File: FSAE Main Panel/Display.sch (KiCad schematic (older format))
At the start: 92 parts, among them Q501 SI2308CDS-T1-GE3, Q502 SI2308CDS-T1-GE3, U501 TLC6C598, U502 TLC6C5816, U503 TLC6C5816, U504 TLC6C5816

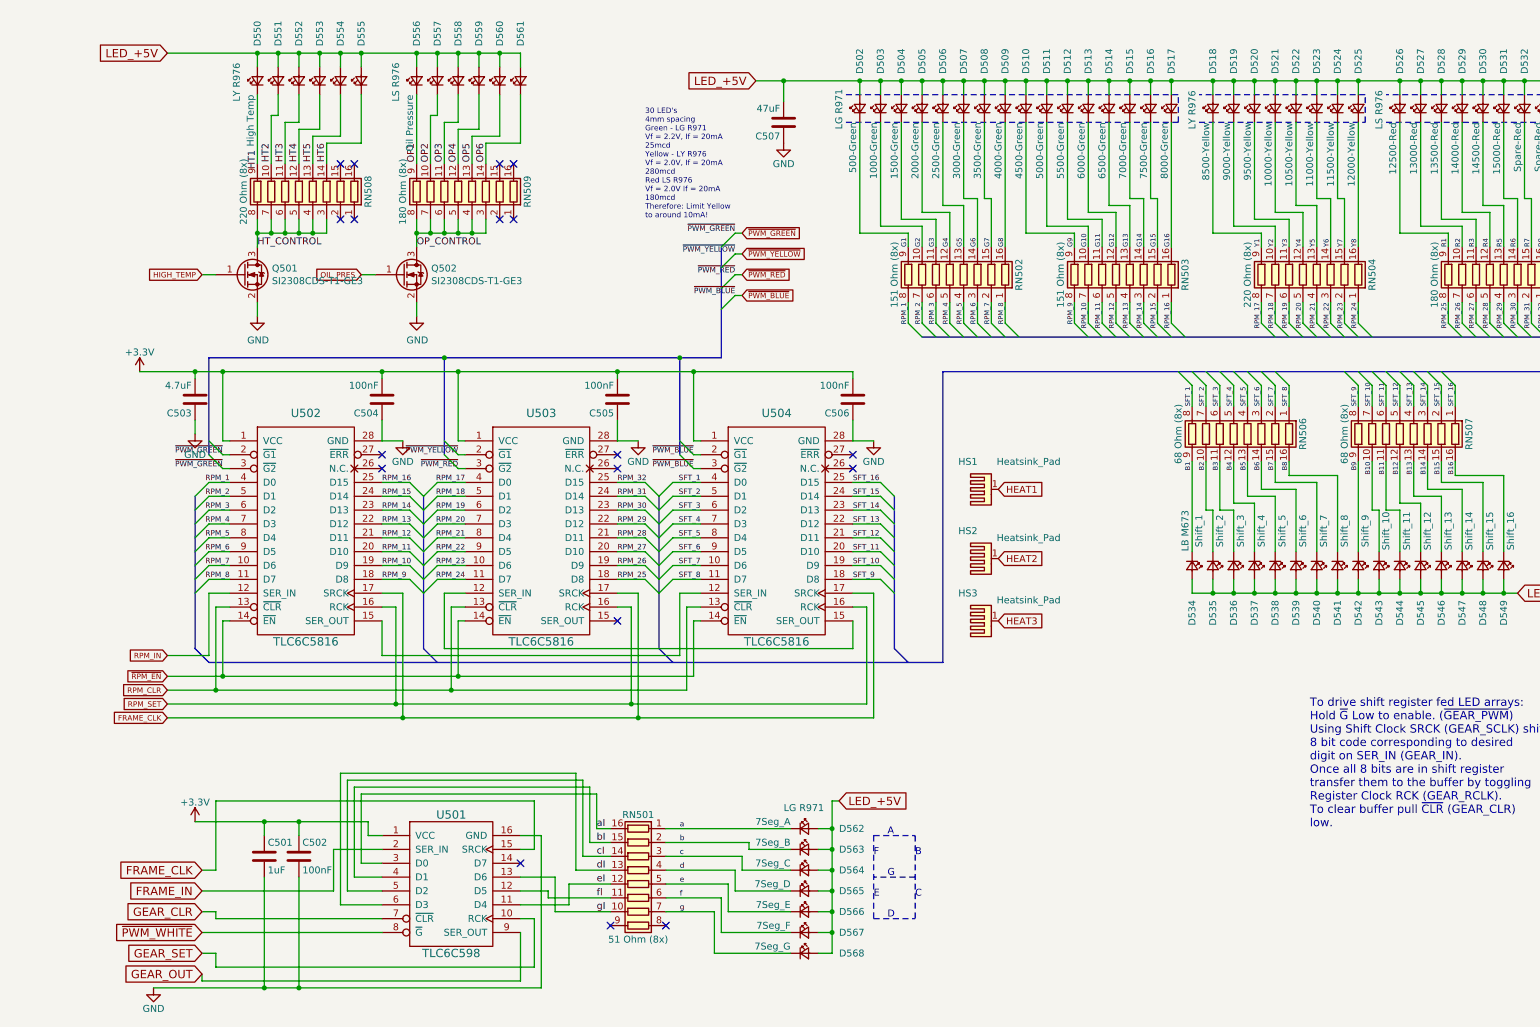
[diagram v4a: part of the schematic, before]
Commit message: Updated attributes and BOM
Standardized the component attributes and BOM.

Some errors were identified and will be corrected in the next board revision
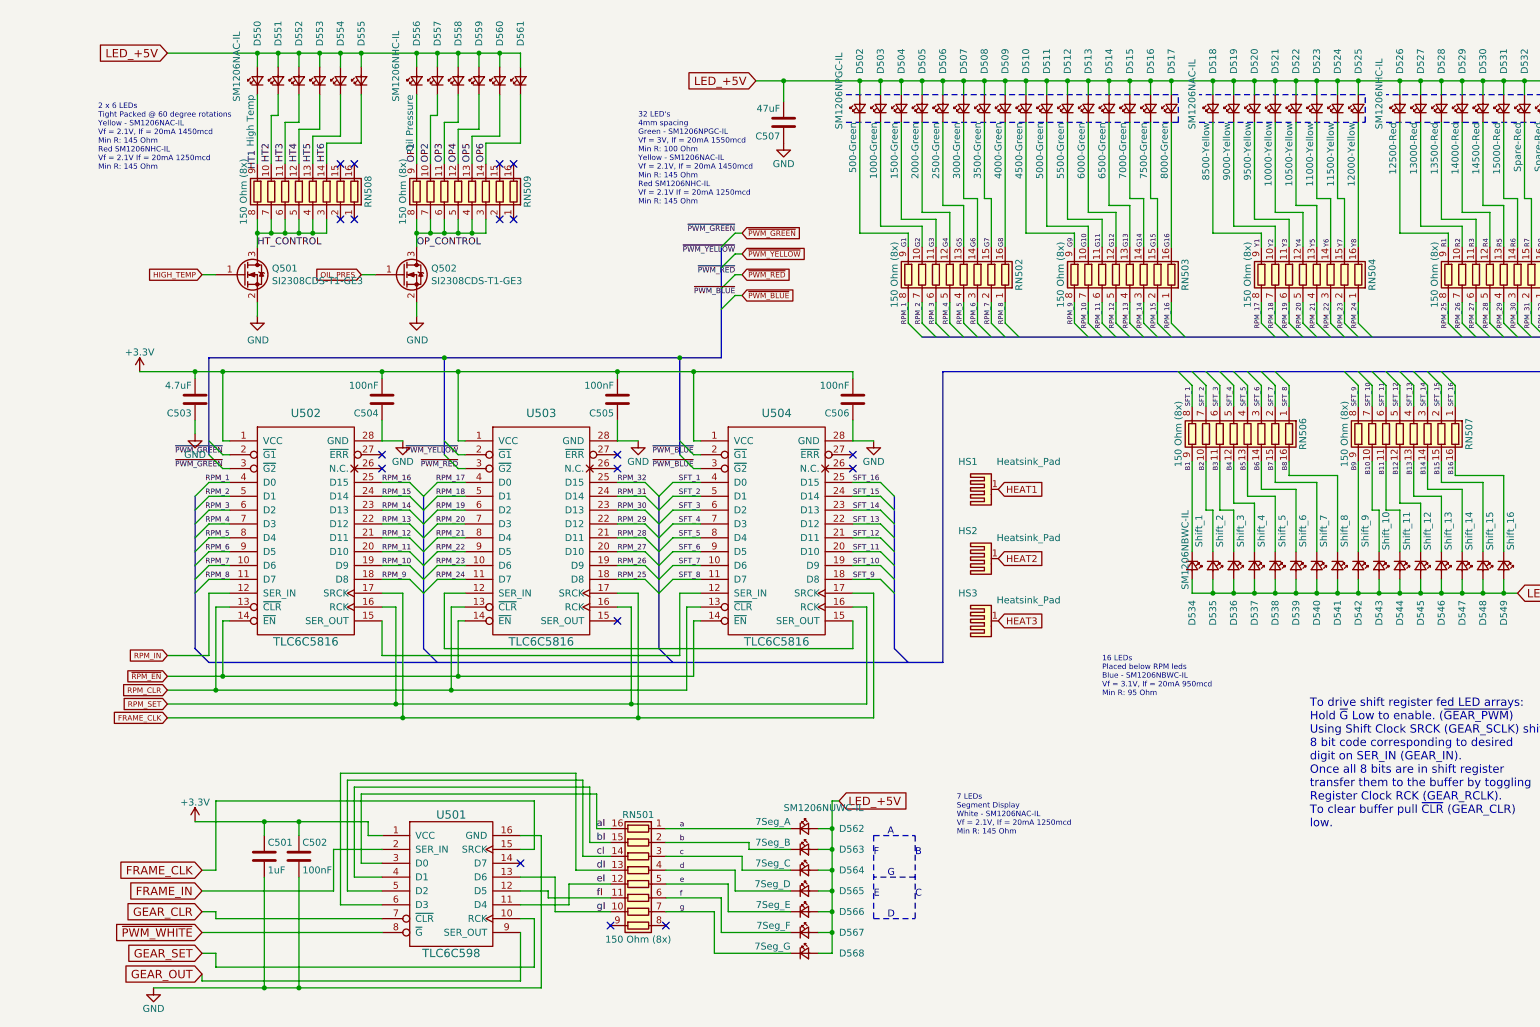
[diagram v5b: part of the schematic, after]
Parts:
- C501: Description Ceramic 1uF 25V X7R 1206 -> CAP CER 1UF 25V X5R 1206; Manufacturer (none) -> KEMET; Part Number (none) -> C1206C105K3PACTU
- C502, C504, C505, C506: Description Ceramic 0.1uF 10V X7R 1206 -> CAP CER 0.1UF 25V X7R 1206; Manufacturer (none) -> KEMET; Part Number (none) -> C1206F104K3RACTU
- C503: Description Ceramic 4.7uF 10V X5R 1206 -> CAP CER 4.7UF 25V X5R 1206; Manufacturer (none) -> KEMET; Part Number (none) -> C1206C475K3PACTU
- C507: Description Ceramic 47uF 10V X5R 1206 -> CAP CER 47UF 10V X5R 1206; Manufacturer (none) -> Murata; Part Number (none) -> GRT31CR61A476KE13L
- D502, D503, D504, D505, D506, D507, D508, D509, D510, D511, D512, D513, D514, D515, D516, D517: value LG R971 -> SM1206NPGC-IL; Description (none) -> LED GREEN CLEAR 1206 SMD; Manufacturer Kingbright -> Bivar; Part Number APD3224ZGCK-F01 -> SM1206NPGC-IL
- D518, D519, D520, D521, D522, D523, D524, D525, D550, D551, D552, D553, D554, D555: value LY R976 -> SM1206NAC-IL; Description (none) -> LED AMBER CLEAR 1206 SMD; Manufacturer Kingbright -> Bivar; Part Number (none) -> SM1206NAC-IL
- D526, D527, D528, D529, D530, D531, D532, D533, D556, D557, D558, D559, D560, D561: value LS R976 -> SM1206NHC-IL; Manufacturer Kingbright -> Bivar
- D534, D535, D536, D537, D538, D539, D540, D541, D542, D543, D544, D545, D546, D547, D548, D549: value LB M673 -> SM1206NBWC-IL; Description (none) -> LED BLUE CLEAR 1206 SMD; Manufacturer Kingbright -> Bivar; Part Number (none) -> SM1206NBWC-IL
- D562, D563, D564, D565, D566, D567, D568: value LG R971 -> SM1206NUWC-IL; Description (none) -> LED WHITE DIFFUSED 1206 SMD; Manufacturer Kingbright -> Bivar; Part Number APD3224ZGCK-F01 -> SM1206NUWC-IL
- HS1, HS2, HS3: Description (none) -> Pad for routing; Manufacturer (none) -> N/A; Part Number (none) -> N/A
- Q501, Q502: Description (none) -> MOSFET N-CH 60V 2.6A SOT23-3; Manufacturer (none) -> Vishay; Part Number (none) -> SI2308CDS-T1-GE3
- RN501: value 51 Ohm (8x) -> 150 Ohm (8x); footprint Housings_SOIC:SOIC-16_3.9x9.9mm_Pitch1.27mm -> Bourns 4800P:Bourns 4800P SOM-16; Description (none) -> RES ARRAY 8 RES 150 OHM 16SOIC; Manufacturer (none) -> Bourns; Part Number 4816P-1-510LF -> 4816P-1-151LF
- RN502, RN503: value 151 Ohm (8x) -> 150 Ohm (8x); Description (none) -> RES ARRAY 8 RES 150 OHM 16SOIC; Manufacturer (none) -> Bourns; Part Number 4816P-1-151 -> 4816P-1-151LF
- RN504, RN508: value 220 Ohm (8x) -> 150 Ohm (8x); Description (none) -> RES ARRAY 8 RES 150 OHM 16SOIC; Manufacturer (none) -> Bourns; Part Number 4816P-1-221LF -> 4816P-1-151LF
- RN505, RN509: value 180 Ohm (8x) -> 150 Ohm (8x); Description (none) -> RES ARRAY 8 RES 150 OHM 16SOIC; Manufacturer (none) -> Bourns; Part Number 4816P-1-181LF -> 4816P-1-151LF
- RN506, RN507: value 68 Ohm (8x) -> 150 Ohm (8x); Description (none) -> RES ARRAY 8 RES 150 OHM 16SOIC; Manufacturer (none) -> Bourns; Part Number 4816P-1-680LF -> 4816P-1-151LF
- U501: Description (none) -> IC LED DRIVER PS 50MA 16TSSOP; Manufacturer Texas Instruments -> TI; Part Number (none) -> TLC6C598QPWRQ1
- U502, U503, U504: Description (none) -> TLC6C5816 PROD VERSION; Manufacturer (none) -> TI; Part Number (none) -> TLC6C5816QPWPRQ1
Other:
- note added: "16 LEDs\nPlaced below RPM leds\nBlue - SM1206NBWC-IL\nVf = 3.1V, If = 20mA 950mcd\nMin R: 95 Ohm\n"
- note added: "2 x 6 LEDs\nTight Packed @ 60 degree rotations\nYellow - SM1206NAC-IL\nVf = 2.1V, If = 20mA 1450mcd\nMin R: 145 Ohm\nRed SM1206NHC-IL\nVf = 2.1V If = 20mA 1250mcd\nMin R: 145 Ohm"
- note added: "32 LED's\n4mm spacing\nGreen - SM1206NPGC-IL\nVf = 3V, If = 20mA 1550mcd\nMin R: 100 Ohm\nYellow - SM1206NAC-IL\nVf = 2.1V, If = 20mA 1450mcd\nMin R: 145 Ohm\nRed SM1206NHC-IL\nVf = 2.1V If = 20mA 1250mcd\nMin R: 145 Ohm"
- note added: "7 LEDs\nSegment Display\nWhite - SM1206NAC-IL\nVf = 2.1V, If = 20mA 1250mcd\nMin R: 145 Ohm\n"
- note removed: "30 LED's\n4mm spacing\nGreen - LG R971\nVf = 2.2V, If = 20mA\n25mcd\nYellow - LY R976\nVf = 2.0V, If = 20mA\n280mcd\nRed LS R976\nVf = 2.0V If = 20mA\n180mcd\nTherefore: Limit Yellow\nto around 10mA!"
